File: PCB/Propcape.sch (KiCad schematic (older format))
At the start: 15 parts, among them P1 CONN_4, P2 CONN_20, P3 CONN_20, P8 BBB_P8, P9 BBB_P9, U1 P8X32A, U2 24C512, U3 LSM303, U4 TMP36, X1 CRYSTAL

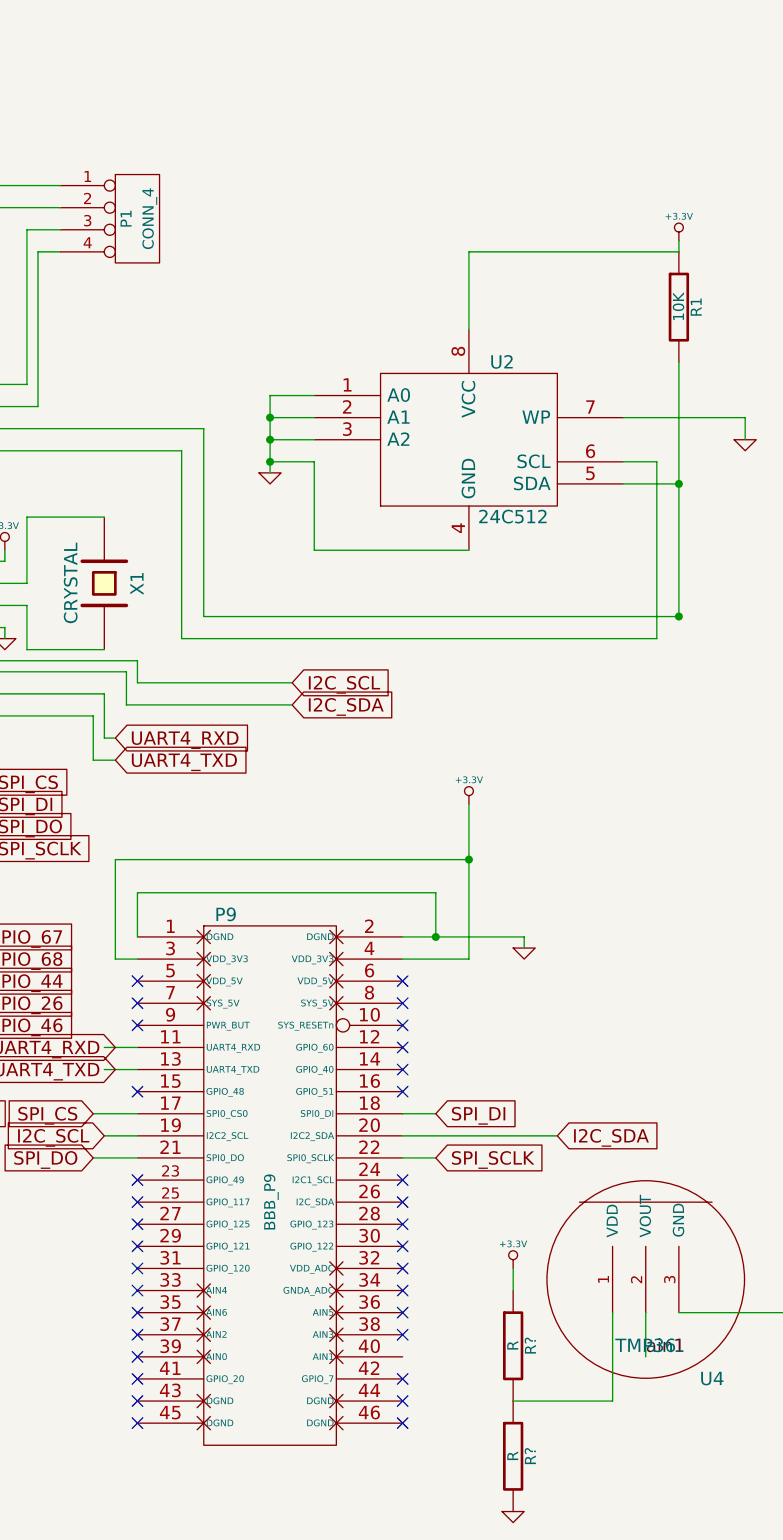
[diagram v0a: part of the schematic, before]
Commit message: send to oshpark for manufacture (v1) Added pmod connector v2 (not in v1).
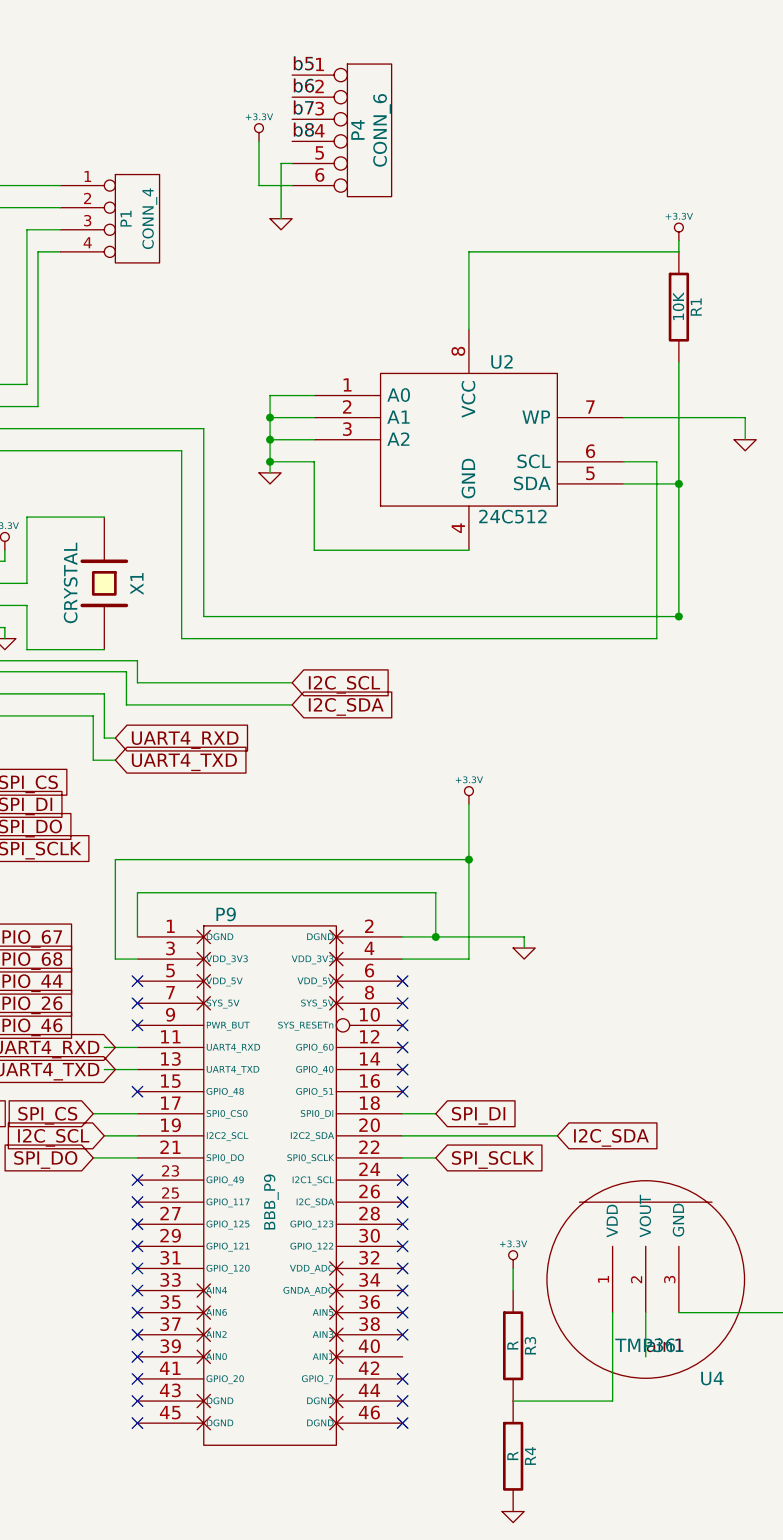
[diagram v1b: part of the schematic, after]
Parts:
- added P4: CONN_6, symbol CONN_6
- gave numbers to parts that had none: 2
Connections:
- net +3.3V: now also P4.6
- net GND: now also P4.5
- net b5: now also P4.1
- net b6: now also P4.2
- net b7: now also P4.3
- net b8: now also P4.4

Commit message: new gerber files and drill files
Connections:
- net ain1: now also P9.40 (AIN1)
